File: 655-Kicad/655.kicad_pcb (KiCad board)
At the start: 2 copper layers, 322.6 x 100 mm, 168 parts, among them IC1 ATMEGA32U4, J1 USBMINI_B05, P1 CONN_1, P2 CONN_1, P3 CONN_1, P4 CONN_1, P5 CONN_1, P6 CONN_1, SW0:0 F0, SW0:1 CTRL, SW0:10 CMD, SW0:11 ALT, SW0:12 CTRL, SW0:13 ←, SW0:14 ↓, SW0:15 →, SW0:2 ALT, SW0:3 CMD, SW0:7 SPACE, SW1:0 F1, SW1:1 SHIFT, SW1:10 ,, SW1:11 ., SW1:12 ?, SW1:13 SHIFT, SW1:14 ↑, SW1:15 END, SW1:3 Z, SW1:4 X, SW1:5 C, SW1:6 V, SW1:7 B, SW1:8 N, SW1:9 M, SW2:0 F2, SW2:1 CAPS, SW2:10 L, SW2:11 ;, SW2:12 ', SW2:14 ENTER, SW2:15 PGDWN, SW2:2 A, SW2:3 S, SW2:4 D, SW2:5 F, SW2:6 G, SW2:7 H, SW2:8 J, SW2:9 K, SW3:0 F3, SW3:1 TAB, SW3:10 O, SW3:11 P, SW3:12 {, SW3:13 }, SW3:14 BCKSL, SW3:15 PGUP, SW3:2 Q, SW3:3 W, SW3:4 E, SW3:5 R, SW3:6 T, SW3:7 Y, SW3:8 U, SW3:9 I, SW4:0 F4, SW4:1 TILDE, SW4:10 9, SW4:11 0, SW4:12 -, SW4:13 =, SW4:14 BCKSP, SW4:15 ESC, SW4:2 1, SW4:3 2, SW4:4 3, SW4:5 4, SW4:6 5, SW4:7 6, SW4:8 7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

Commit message: thinner cut line, moved in cut line, pdf printing files
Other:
- board size 322.6 x 100 mm -> 321.4 x 97.1 mm
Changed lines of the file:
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@@
       (net 20 GND))
   )
-  (gr_line (start 422.9608 152.4508) (end 100.4062 152.4508) (angle 90) (layer Edge.Cuts) (width 0.381))
-  (gr_line (start 422.9608 252.4506) (end 422.9608 152.4508) (angle 90) (layer Edge.Cuts) (width 0.381))
-  (gr_line (start 100.4062 252.4506) (end 422.9608 252.4506) (angle 90) (layer Edge.Cuts) (width 0.381))
-  (gr_line (start 100.4062 152.4762) (end 100.4062 252.4506) (angle 90) (layer Edge.Cuts) (width 0.381))
+  (gr_line (start 421.76 152.4508) (end 100.4062 152.4508) (angle 90) (layer Edge.Cuts) (width 0.1))
+  (gr_line (start 421.767 249.525) (end 421.767 152.4508) (angle 90) (layer Edge.Cuts) (width 0.1))
+  (gr_line (start 100.4062 249.5296) (end 421.765 249.5296) (angle 90) (layer Edge.Cuts) (width 0.1))
+  (gr_line (start 100.4062 152.46) (end 100.4062 249.52) (angle 90) (layer Edge.Cuts) (width 0.1))
   (gr_line (start 406.5542 169.4032) (end 406.5542 155.4025) (layer Eco2.User) (width 0.1))
   (gr_line (start 420.5552 169.4032) (end 406.5542 169.4032) (layer Eco2.User) (width 0.1))

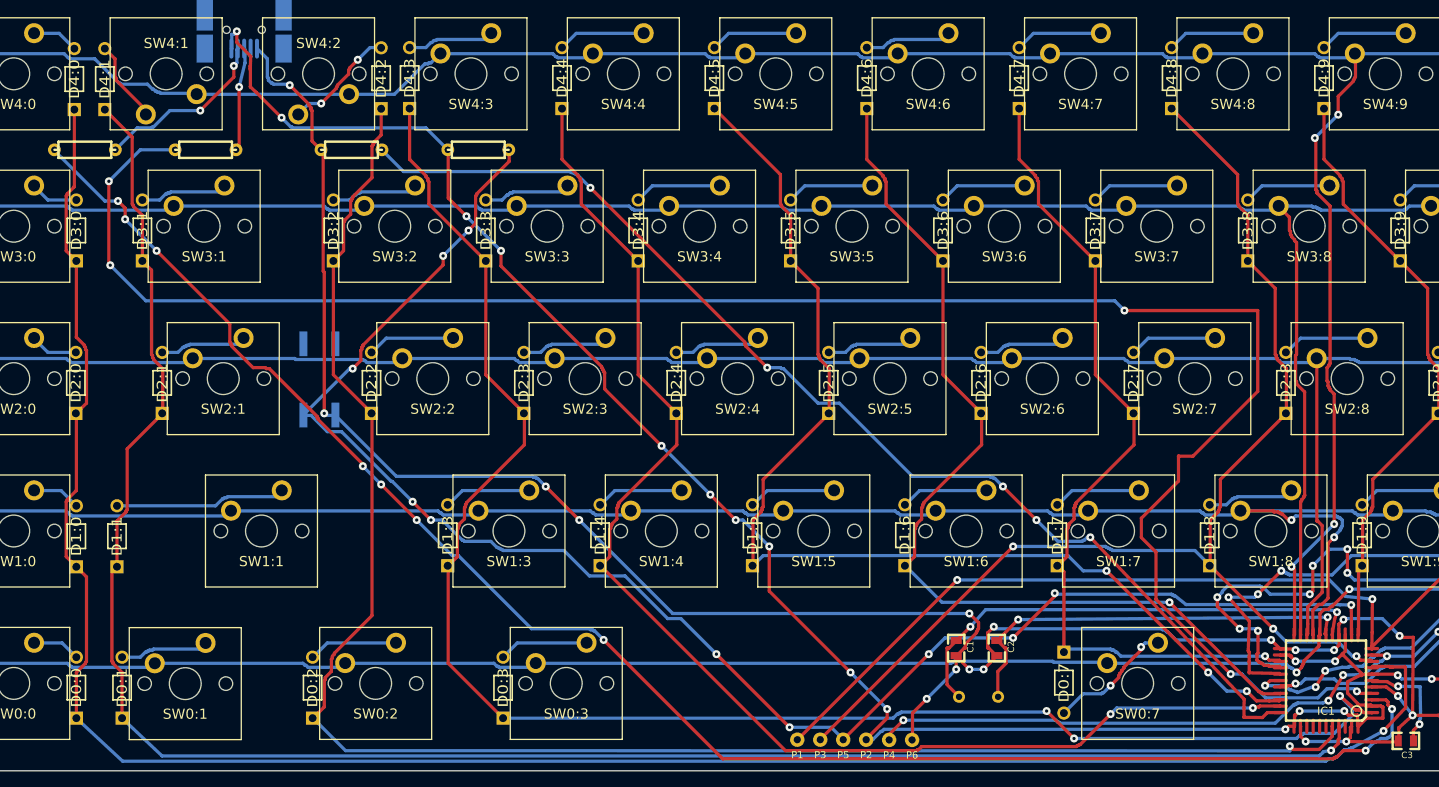
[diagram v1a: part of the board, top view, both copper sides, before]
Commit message: change resistor footprints to 0805R, add caps led
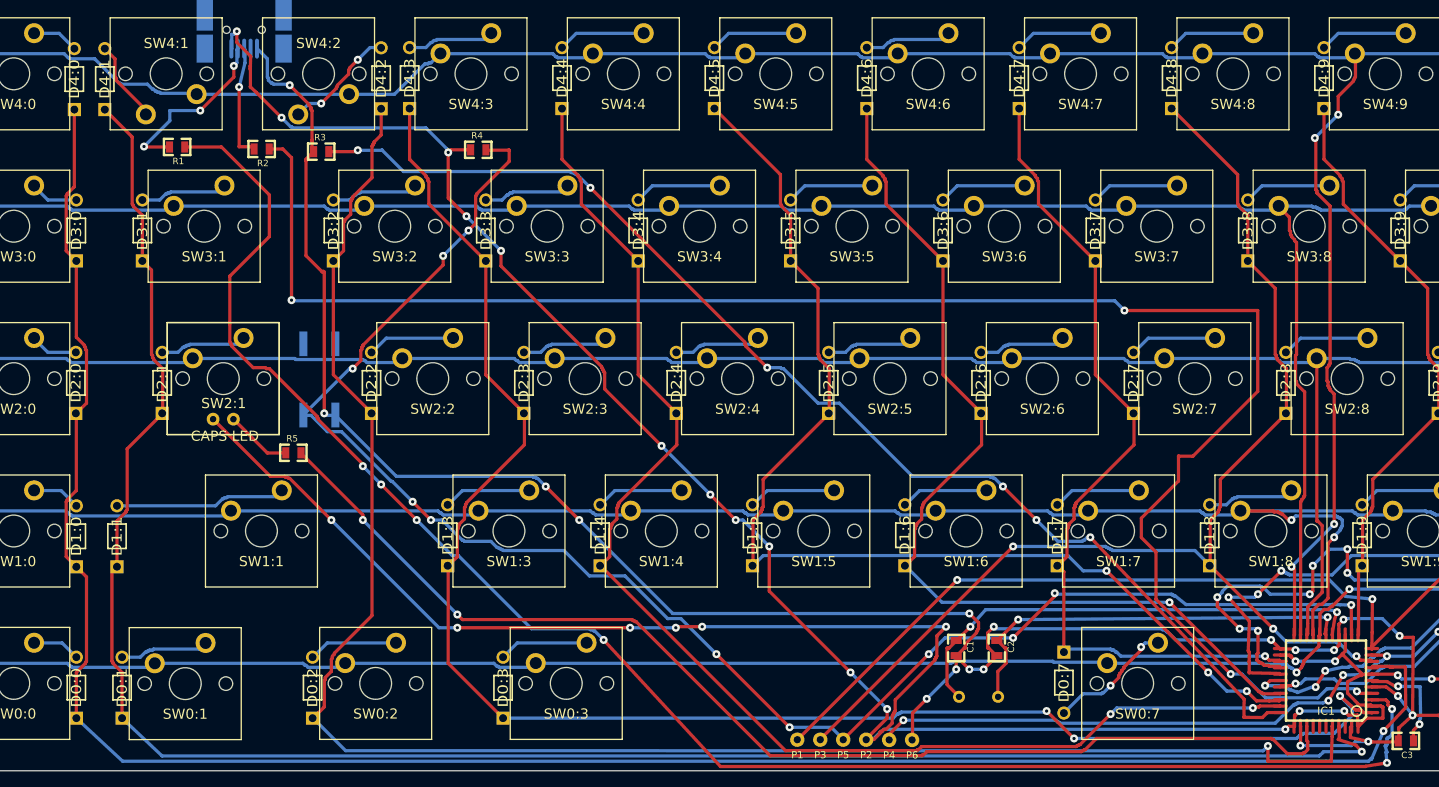
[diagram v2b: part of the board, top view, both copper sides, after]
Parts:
- added D1: CAPS LED, mx1a:MX1A-led, F.Cu at (135.0, 200.5)
- added R5: 300, 0805:0805R, F.Cu at (143.7, 209.8)
- R1, R2, R3, R4: footprint res:resistor -> 0805:0805R
- moved R1 11.5 mm to (129.2, 171.6), turned to 180 degrees
- moved R2 7.01 mm to (139.8, 171.8), turned to 180 degrees
- moved R3 3.79 mm to (147.2, 172.1)
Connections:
- IC1 pad 36: (no net) -> /caps_led
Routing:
- net /caps_led: track 0.00 -> 146.8 mm, vias 0 -> 2
- net VCC: track 266.4 -> 391.5 mm, vias 17 -> 24
- net Net-(IC1-Pad4): track 243.0 -> 219.1 mm, vias 5 -> 4
- net Net-(D1-Pad2): track 0.00 -> 8.30 mm
- net Net-(IC1-Pad33): track 144.2 -> 151.0 mm, vias 5 -> 6
- net /COL1: track 239.1 -> 244.6 mm
- net GND: track 296.4 -> 300.2 mm
- net /COL2: track 215.7 -> 219.5 mm
- net /RES: track 204.2 -> 207.2 mm
- net Net-(IC1-Pad3): track 209.1 -> 211.8 mm, vias 9 -> 6
- net /COL0: track 260.5 -> 262.0 mm
- net Net-(J1-Pad3): track 13.0 -> 14.4 mm
- net Net-(J1-Pad2): track 22.4 -> 22.6 mm, vias 2 -> 3

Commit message: ground plane attempt
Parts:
- moved C1 42.0 mm to (268.5, 232.2), turned to 90 degrees
- moved C2 37.2 mm to (268.5, 239.3)
- moved X1 34.4 mm to (263.4, 235.5), turned to 270 degrees
- moved C3 8.07 mm to (290.8, 246.4)
- moved IC1 6.59 mm to (279.1, 236.5), turned to 270 degrees
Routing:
- net /ROW4: track 394.1 -> 0.00 mm, vias 4 -> 0
- net VCC: track 391.5 -> 0.00 mm, vias 24 -> 0
- net /ROW3: track 368.1 -> 0.00 mm
- net /ROW2: track 347.4 -> 0.00 mm
- net /ROW1: track 341.3 -> 0.00 mm, vias 2 -> 0
- net /ROW0: track 320.8 -> 0.00 mm, vias 5 -> 0
- net GND: track 300.2 -> 0.00 mm, vias 19 -> 0
- net /COL14: track 288.7 -> 0.00 mm, vias 6 -> 0
- net /COL15: track 288.1 -> 0.00 mm, vias 5 -> 0
- net /COL0: track 262.0 -> 0.00 mm, vias 1 -> 0
- net /COL1: track 244.6 -> 0.00 mm, vias 1 -> 0
- net /COL2: track 219.5 -> 0.00 mm, vias 1 -> 0
- net Net-(IC1-Pad4): track 219.1 -> 0.00 mm, vias 4 -> 0
- net Net-(IC1-Pad3): track 211.8 -> 0.00 mm, vias 6 -> 0
- net /COL13: track 209.5 -> 0.00 mm, vias 9 -> 0
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- added copper zone on B.Cu, net GND
- added copper zone on F.Cu, net GND

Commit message: fixing up matrix, re zoning, no routes
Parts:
- removed P1, P2, P3, P4, P5, P6: CONN_1, pin:pad
- moved R1 164.3 mm to (283.2, 228.9), turned to 0 degrees
- moved R3 160.3 mm to (289.6, 245.9), turned to 180 degrees
- moved R2 150.6 mm to (279.1, 228.9)
- moved R4 143.3 mm to (293.9, 238.3), turned to 90 degrees
- moved C7 34.2 mm to (269.5, 245.9), turned to 180 degrees
- moved C6 31.3 mm to (271.0, 228.9), turned to 180 degrees
- moved C3 23.6 mm to (275.1, 228.9)
- moved C8 12.3 mm to (287.3, 228.9), turned to 180 degrees
- moved C4 6.70 mm to (293.9, 234.2)
- moved C5 3.02 mm to (293.9, 242.3)
- moved X1 2.74 mm to (264.4, 238.0)
- moved C1 2.54 mm to (268.5, 234.7)
- moved C2 2.29 mm to (268.5, 241.6)
- moved IC1 1.93 mm to (279.9, 238.3)
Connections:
- net /RES renamed Net-(IC1-Pad13)
- D0:0 pad 2: /COL0 -> /row0
- D0:1 pad 2: /COL1 -> /row0
- D0:10 pad 2: /COL10 -> /row0
- D0:11 pad 2: /COL11 -> /row0
- D0:12 pad 2: /COL12 -> /row0
- D0:13 pad 2: /COL13 -> /row0
- D0:14 pad 2: /COL14 -> /row0
- D0:15 pad 2: /COL15 -> /row0
- D0:2 pad 2: /COL2 -> /row0
- D0:3 pad 2: /COL3 -> /row0
- D0:7 pad 2: /COL7 -> /row0
- D1:0 pad 2: /COL0 -> /row1
- D1:1 pad 2: /COL1 -> /row1
- D1:10 pad 2: /COL10 -> /row1
- D1:11 pad 2: /COL11 -> /row1
- D1:12 pad 2: /COL12 -> /row1
- D1:13 pad 2: /COL13 -> /row1
- D1:14 pad 2: /COL14 -> /row1
- D1:15 pad 2: /COL15 -> /row1
- D1:3 pad 2: /COL3 -> /row1
- D1:4 pad 2: /COL4 -> /row1
- D1:5 pad 2: /COL5 -> /row1
- D1:6 pad 2: /COL6 -> /row1
- D1:7 pad 2: /COL7 -> /row1
- D1:8 pad 2: /COL8 -> /row1
- D1:9 pad 2: /COL9 -> /row1
- D2:0 pad 2: /COL0 -> /row2
- D2:1 pad 2: /COL1 -> /row2
- D2:10 pad 2: /COL10 -> /row2
- D2:11 pad 2: /COL11 -> /row2
- D2:12 pad 2: /COL12 -> /row2
- D2:14 pad 2: /COL14 -> /row2
- D2:15 pad 2: /COL15 -> /row2
- D2:2 pad 2: /COL2 -> /row2
- D2:3 pad 2: /COL3 -> /row2
- D2:4 pad 2: /COL4 -> /row2
- D2:5 pad 2: /COL5 -> /row2
- D2:6 pad 2: /COL6 -> /row2
- D2:7 pad 2: /COL7 -> /row2
- D2:8 pad 2: /COL8 -> /row2
- D2:9 pad 2: /COL9 -> /row2
- D3:0 pad 2: /COL0 -> /row3
- D3:1 pad 2: /COL1 -> /row3
- D3:10 pad 2: /COL10 -> /row3
- D3:11 pad 2: /COL11 -> /row3
- D3:12 pad 2: /COL12 -> /row3
- D3:13 pad 2: /COL13 -> /row3
- D3:14 pad 2: /COL14 -> /row3
- D3:15 pad 2: /COL15 -> /row3
- D3:2 pad 2: /COL2 -> /row3
- D3:3 pad 2: /COL3 -> /row3
- D3:4 pad 2: /COL4 -> /row3
- D3:5 pad 2: /COL5 -> /row3
- D3:6 pad 2: /COL6 -> /row3
- D3:7 pad 2: /COL7 -> /row3
- D3:8 pad 2: /COL8 -> /row3
- D3:9 pad 2: /COL9 -> /row3
- D4:0 pad 2: /COL0 -> /row4
- D4:1 pad 2: /COL1 -> /row4
- D4:10 pad 2: /COL10 -> /row4
- D4:11 pad 2: /COL11 -> /row4
- D4:12 pad 2: /COL12 -> /row4
- D4:13 pad 2: /COL13 -> /row4
- D4:14 pad 2: /COL14 -> /row4
- D4:15 pad 2: /COL15 -> /row4
- D4:2 pad 2: /COL2 -> /row4
- D4:3 pad 2: /COL3 -> /row4
- D4:4 pad 2: /COL4 -> /row4
- D4:5 pad 2: /COL5 -> /row4
- D4:6 pad 2: /COL6 -> /row4
- D4:7 pad 2: /COL7 -> /row4
- D4:8 pad 2: /COL8 -> /row4
- D4:9 pad 2: /COL9 -> /row4
- IC1 pad 1: /COL3 -> /col10
- IC1 pad 10: /COL15 -> /col7
- IC1 pad 11: /COL14 -> /col6
- IC1 pad 12: /COL9 -> /col0
- IC1 pad 18: /ROW0 -> /col1
- IC1 pad 19: /ROW1 -> /col2
- IC1 pad 20: /ROW2 -> /col3
- IC1 pad 21: /ROW3 -> /col4
- IC1 pad 22: /ROW4 -> /col5
- IC1 pad 25: /COL7 -> (no net)
- IC1 pad 26: /COL13 -> (no net)
- IC1 pad 27: /COL12 -> /row4
- IC1 pad 28: /COL11 -> /row3
- IC1 pad 29: /COL10 -> /row2
- IC1 pad 30: /COL6 -> /row1
- IC1 pad 31: /COL5 -> /row0
- IC1 pad 32: /COL4 -> /col15
- IC1 pad 38: (no net) -> /col15
- IC1 pad 39: (no net) -> /col14
- IC1 pad 40: /COL2 -> /col13
- IC1 pad 41: /COL1 -> /col11
- IC1 pad 8: /COL0 -> /col9
- IC1 pad 9: /COL8 -> /col8
- SW0:0 pad 1: /ROW0 -> Net-(D0:0-Pad1)
- SW0:0 pad 2: Net-(D0:0-Pad1) -> /col0
- SW0:1 pad 1: /ROW0 -> Net-(D0:1-Pad1)
- SW0:1 pad 2: Net-(D0:1-Pad1) -> /col1
- SW0:10 pad 1: /ROW0 -> Net-(D0:10-Pad1)
- SW0:10 pad 2: Net-(D0:10-Pad1) -> /col10
- SW0:11 pad 1: /ROW0 -> Net-(D0:11-Pad1)
- SW0:11 pad 2: Net-(D0:11-Pad1) -> /col11
- SW0:12 pad 1: /ROW0 -> Net-(D0:12-Pad1)
- SW0:12 pad 2: Net-(D0:12-Pad1) -> /col12
- SW0:13 pad 1: /ROW0 -> Net-(D0:13-Pad1)
- SW0:13 pad 2: Net-(D0:13-Pad1) -> /col13
- SW0:14 pad 1: /ROW0 -> Net-(D0:14-Pad1)
- SW0:14 pad 2: Net-(D0:14-Pad1) -> /col14
- SW0:15 pad 1: /ROW0 -> Net-(D0:15-Pad1)
- SW0:15 pad 2: Net-(D0:15-Pad1) -> /col15
- SW0:2 pad 1: /ROW0 -> Net-(D0:2-Pad1)
- SW0:2 pad 2: Net-(D0:2-Pad1) -> /col2
- SW0:3 pad 1: /ROW0 -> Net-(D0:3-Pad1)
- SW0:3 pad 2: Net-(D0:3-Pad1) -> /col3
- SW0:7 pad 1: /ROW0 -> Net-(D0:7-Pad1)
- SW0:7 pad 2: Net-(D0:7-Pad1) -> /col7
- SW1:0 pad 1: /ROW1 -> Net-(D1:0-Pad1)
- SW1:0 pad 2: Net-(D1:0-Pad1) -> /col0
- SW1:1 pad 1: /ROW1 -> Net-(D1:1-Pad1)
- SW1:1 pad 2: Net-(D1:1-Pad1) -> /col1
- SW1:10 pad 1: /ROW1 -> Net-(D1:10-Pad1)
- SW1:10 pad 2: Net-(D1:10-Pad1) -> /col10
- SW1:11 pad 1: /ROW1 -> Net-(D1:11-Pad1)
- SW1:11 pad 2: Net-(D1:11-Pad1) -> /col11
- SW1:12 pad 1: /ROW1 -> Net-(D1:12-Pad1)
- SW1:12 pad 2: Net-(D1:12-Pad1) -> /col12
- SW1:13 pad 1: /ROW1 -> Net-(D1:13-Pad1)
- SW1:13 pad 2: Net-(D1:13-Pad1) -> /col13
- SW1:14 pad 1: /ROW1 -> Net-(D1:14-Pad1)
- SW1:14 pad 2: Net-(D1:14-Pad1) -> /col14
- SW1:15 pad 1: /ROW1 -> Net-(D1:15-Pad1)
- SW1:15 pad 2: Net-(D1:15-Pad1) -> /col15
- SW1:3 pad 1: /ROW1 -> Net-(D1:3-Pad1)
- SW1:3 pad 2: Net-(D1:3-Pad1) -> /col3
- SW1:4 pad 1: /ROW1 -> Net-(D1:4-Pad1)
- SW1:4 pad 2: Net-(D1:4-Pad1) -> /col4
- SW1:5 pad 1: /ROW1 -> Net-(D1:5-Pad1)
- SW1:5 pad 2: Net-(D1:5-Pad1) -> /col5
- SW1:6 pad 1: /ROW1 -> Net-(D1:6-Pad1)
- SW1:6 pad 2: Net-(D1:6-Pad1) -> /col6
- SW1:7 pad 1: /ROW1 -> Net-(D1:7-Pad1)
- SW1:7 pad 2: Net-(D1:7-Pad1) -> /col7
- SW1:8 pad 1: /ROW1 -> Net-(D1:8-Pad1)
- SW1:8 pad 2: Net-(D1:8-Pad1) -> /col8
- SW1:9 pad 1: /ROW1 -> Net-(D1:9-Pad1)
- SW1:9 pad 2: Net-(D1:9-Pad1) -> /col9
- SW2:0 pad 1: /ROW2 -> Net-(D2:0-Pad1)
- SW2:0 pad 2: Net-(D2:0-Pad1) -> /col0
- SW2:1 pad 1: /ROW2 -> Net-(D2:1-Pad1)
- SW2:1 pad 2: Net-(D2:1-Pad1) -> /col1
- SW2:10 pad 1: /ROW2 -> Net-(D2:10-Pad1)
- SW2:10 pad 2: Net-(D2:10-Pad1) -> /col10
- SW2:11 pad 1: /ROW2 -> Net-(D2:11-Pad1)
- SW2:11 pad 2: Net-(D2:11-Pad1) -> /col11
- SW2:12 pad 1: /ROW2 -> Net-(D2:12-Pad1)
- SW2:12 pad 2: Net-(D2:12-Pad1) -> /col12
- SW2:14 pad 1: /ROW2 -> Net-(D2:14-Pad1)
- SW2:14 pad 2: Net-(D2:14-Pad1) -> /col14
- SW2:15 pad 1: /ROW2 -> Net-(D2:15-Pad1)
- SW2:15 pad 2: Net-(D2:15-Pad1) -> /col15
- SW2:2 pad 1: /ROW2 -> Net-(D2:2-Pad1)
- SW2:2 pad 2: Net-(D2:2-Pad1) -> /col2
- SW2:3 pad 1: /ROW2 -> Net-(D2:3-Pad1)
- SW2:3 pad 2: Net-(D2:3-Pad1) -> /col3
- SW2:4 pad 1: /ROW2 -> Net-(D2:4-Pad1)
- SW2:4 pad 2: Net-(D2:4-Pad1) -> /col4
- SW2:5 pad 1: /ROW2 -> Net-(D2:5-Pad1)
- SW2:5 pad 2: Net-(D2:5-Pad1) -> /col5
- SW2:6 pad 1: /ROW2 -> Net-(D2:6-Pad1)
- SW2:6 pad 2: Net-(D2:6-Pad1) -> /col6
- SW2:7 pad 1: /ROW2 -> Net-(D2:7-Pad1)
- SW2:7 pad 2: Net-(D2:7-Pad1) -> /col7
- SW2:8 pad 1: /ROW2 -> Net-(D2:8-Pad1)
- SW2:8 pad 2: Net-(D2:8-Pad1) -> /col8
- SW2:9 pad 1: /ROW2 -> Net-(D2:9-Pad1)
- SW2:9 pad 2: Net-(D2:9-Pad1) -> /col9
- SW3:0 pad 1: /ROW3 -> Net-(D3:0-Pad1)
- SW3:0 pad 2: Net-(D3:0-Pad1) -> /col0
- SW3:1 pad 1: /ROW3 -> Net-(D3:1-Pad1)
- SW3:1 pad 2: Net-(D3:1-Pad1) -> /col1
- SW3:10 pad 1: /ROW3 -> Net-(D3:10-Pad1)
- SW3:10 pad 2: Net-(D3:10-Pad1) -> /col10
- SW3:11 pad 1: /ROW3 -> Net-(D3:11-Pad1)
- SW3:11 pad 2: Net-(D3:11-Pad1) -> /col11
- SW3:12 pad 1: /ROW3 -> Net-(D3:12-Pad1)
- SW3:12 pad 2: Net-(D3:12-Pad1) -> /col12
- SW3:13 pad 1: /ROW3 -> Net-(D3:13-Pad1)
- SW3:13 pad 2: Net-(D3:13-Pad1) -> /col13
- SW3:14 pad 1: /ROW3 -> Net-(D3:14-Pad1)
- SW3:14 pad 2: Net-(D3:14-Pad1) -> /col14
- SW3:15 pad 1: /ROW3 -> Net-(D3:15-Pad1)
- SW3:15 pad 2: Net-(D3:15-Pad1) -> /col15
- SW3:2 pad 1: /ROW3 -> Net-(D3:2-Pad1)
- SW3:2 pad 2: Net-(D3:2-Pad1) -> /col2
- SW3:3 pad 1: /ROW3 -> Net-(D3:3-Pad1)
- SW3:3 pad 2: Net-(D3:3-Pad1) -> /col3
- SW3:4 pad 1: /ROW3 -> Net-(D3:4-Pad1)
- SW3:4 pad 2: Net-(D3:4-Pad1) -> /col4
- SW3:5 pad 1: /ROW3 -> Net-(D3:5-Pad1)
- SW3:5 pad 2: Net-(D3:5-Pad1) -> /col5
- SW3:6 pad 1: /ROW3 -> Net-(D3:6-Pad1)
- SW3:6 pad 2: Net-(D3:6-Pad1) -> /col6
- SW3:7 pad 1: /ROW3 -> Net-(D3:7-Pad1)
- SW3:7 pad 2: Net-(D3:7-Pad1) -> /col7
- SW3:8 pad 1: /ROW3 -> Net-(D3:8-Pad1)
- SW3:8 pad 2: Net-(D3:8-Pad1) -> /col8
- SW3:9 pad 1: /ROW3 -> Net-(D3:9-Pad1)
- SW3:9 pad 2: Net-(D3:9-Pad1) -> /col9
- SW4:0 pad 1: /ROW4 -> Net-(D4:0-Pad1)
- SW4:0 pad 2: Net-(D4:0-Pad1) -> /col0
- SW4:1 pad 1: /ROW4 -> Net-(D4:1-Pad1)
- SW4:1 pad 2: Net-(D4:1-Pad1) -> /col1
- SW4:10 pad 1: /ROW4 -> Net-(D4:10-Pad1)
- SW4:10 pad 2: Net-(D4:10-Pad1) -> /col10
- SW4:11 pad 1: /ROW4 -> Net-(D4:11-Pad1)
- SW4:11 pad 2: Net-(D4:11-Pad1) -> /col11
- SW4:12 pad 1: /ROW4 -> Net-(D4:12-Pad1)
- SW4:12 pad 2: Net-(D4:12-Pad1) -> /col12
- SW4:13 pad 1: /ROW4 -> Net-(D4:13-Pad1)
- SW4:13 pad 2: Net-(D4:13-Pad1) -> /col13
- SW4:14 pad 1: /ROW4 -> Net-(D4:14-Pad1)
- SW4:14 pad 2: Net-(D4:14-Pad1) -> /col14
- SW4:15 pad 1: /ROW4 -> Net-(D4:15-Pad1)
- SW4:15 pad 2: Net-(D4:15-Pad1) -> /col15
- SW4:2 pad 1: /ROW4 -> Net-(D4:2-Pad1)
- SW4:2 pad 2: Net-(D4:2-Pad1) -> /col2
- SW4:3 pad 1: /ROW4 -> Net-(D4:3-Pad1)
- SW4:3 pad 2: Net-(D4:3-Pad1) -> /col3
- SW4:4 pad 1: /ROW4 -> Net-(D4:4-Pad1)
- SW4:4 pad 2: Net-(D4:4-Pad1) -> /col4
- SW4:5 pad 1: /ROW4 -> Net-(D4:5-Pad1)
- SW4:5 pad 2: Net-(D4:5-Pad1) -> /col5
- SW4:6 pad 1: /ROW4 -> Net-(D4:6-Pad1)
- SW4:6 pad 2: Net-(D4:6-Pad1) -> /col6
- SW4:7 pad 1: /ROW4 -> Net-(D4:7-Pad1)
- SW4:7 pad 2: Net-(D4:7-Pad1) -> /col7
- SW4:8 pad 1: /ROW4 -> Net-(D4:8-Pad1)
- SW4:8 pad 2: Net-(D4:8-Pad1) -> /col8
- SW4:9 pad 1: /ROW4 -> Net-(D4:9-Pad1)
- SW4:9 pad 2: Net-(D4:9-Pad1) -> /col9
